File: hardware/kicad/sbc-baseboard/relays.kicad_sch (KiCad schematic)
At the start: 30 parts, among them J11 COM/NO/NC, J12 COM/NO/NC, J18 PSU in (isolated), J19 PSU out (isolated), K801 G6K-2F-Y DC5, K802 G6K-2F-Y DC5, K803 JW1FSN-DC5V, Q801 2N7002, Q802 2N7002, Q803 AO3400A, U801 LTV-817

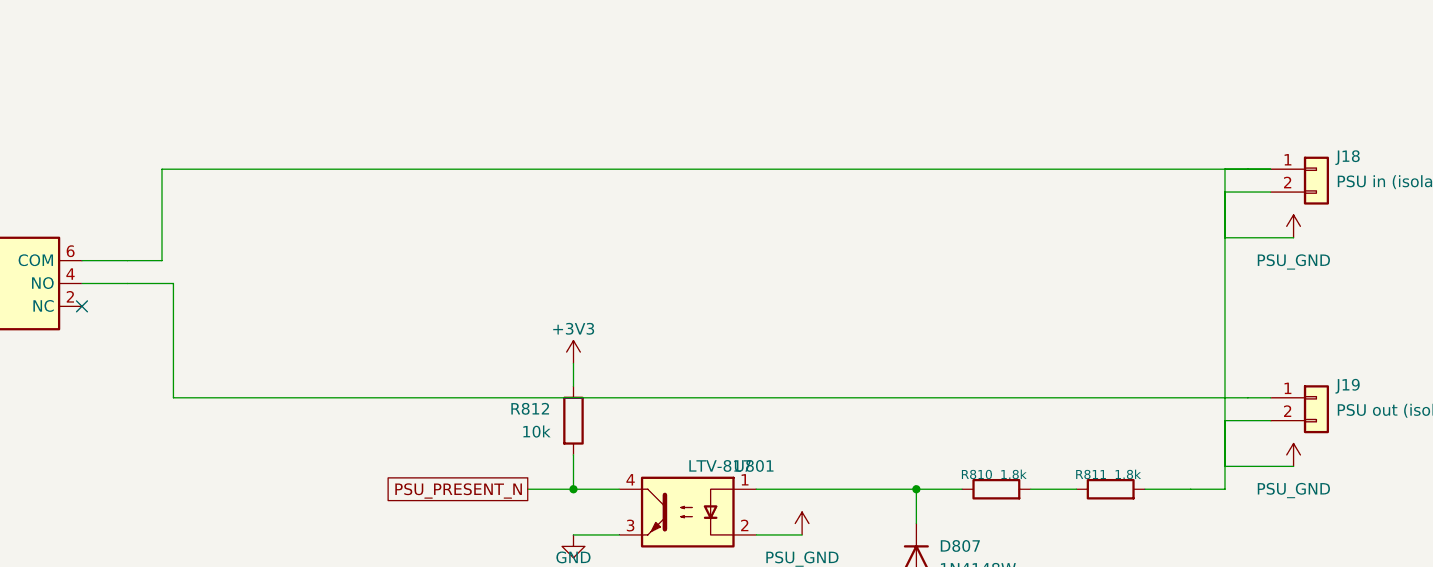
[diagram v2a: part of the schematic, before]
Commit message: USB 2.0 differential pairs named for the router; USB net class; ports aligned
Every USB 2.0 data net is now <base>_P / <base>_N, the suffixes KiCad's PCB
editor pairs up: J1_D, J3_D, PORT1_D..PORT4_D on the receptacle side of each
ESD array; HUB_UP and HUB_DN1..HUB_DN7 at the hub; K64_USB and FTDI_USB at the
chips. All 15 pairs are complete with D+ on _P. The project file gains a USB
net class assigned by pattern (differential geometry to be set from the
stackup). The labels sit at wire ends with their text along the pair's own
wire; routes now run their last leg into a side pin as one wire so a label at
the pin end owns the stretch (Conn join=False keeps a shared stub where two
routes meet at one pin). The USB-A receptacles and their switches move down
1.27 mm so the pairs run straight from the ESD arrays, and the port ESD arrays
move left to make room for the labels. Netlist membership unchanged (356
nets); ERC, geometry, connectivity, layout and reproducibility gates all
clean.

Co-Authored-By: Claude Fable 5.1 <noreply@anthropic.com>
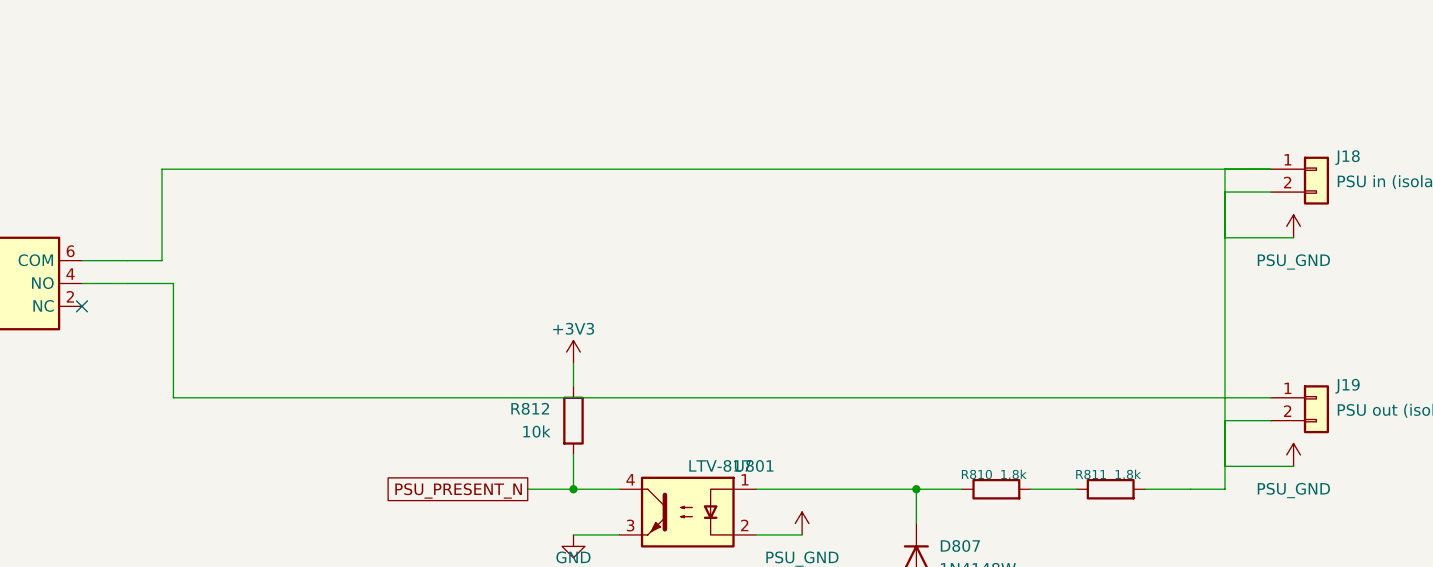
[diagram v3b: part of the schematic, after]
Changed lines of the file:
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@@
 		(pts
 			(xy 171.45 212.09)
-			(xy 292.1 212.09)
-		)
-		(stroke
-			(width 0)
-			(type default)
-		)
-	)
-	(wire
-		(pts
-			(xy 292.1 212.09)
 			(xy 294.64 212.09)
 		)
@@
 		(pts
 			(xy 172.72 237.49)
-			(xy 292.1 237.49)
-		)
-		(stroke
-			(width 0)
-			(type default)
-		)
-	)
-	(wire
-		(pts
-			(xy 292.1 237.49)
 			(xy 294.64 237.49)
 		)
@@
 		(pts
 			(xy 289.56 212.09)
-			(xy 292.1 212.09)
-		)
-		(stroke
-			(width 0)
-			(type default)
-		)
-	)
-	(wire
-		(pts
-			(xy 292.1 212.09)
 			(xy 294.64 212.09)
 		)

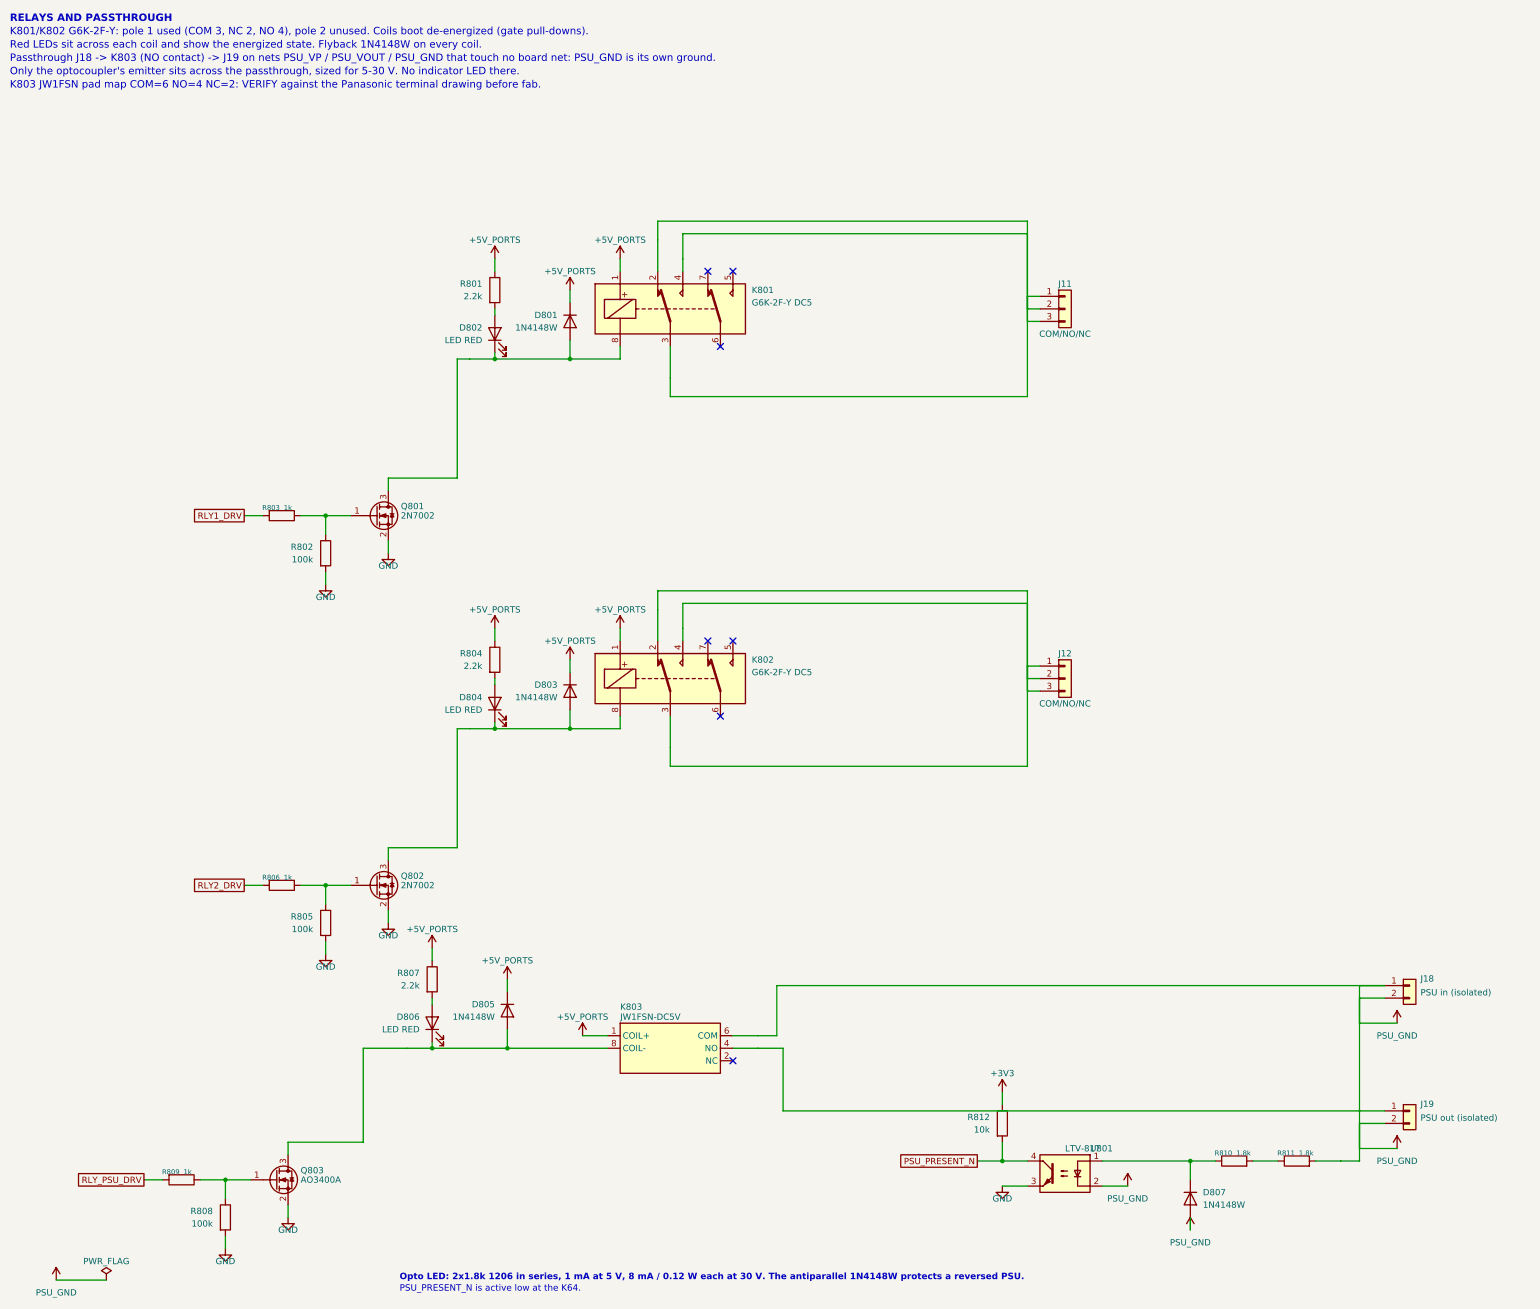
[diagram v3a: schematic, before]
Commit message: Nothing drawn over anything else; FTDI Friend header; DAPLink per FRDM-K64F; 90 ohm USB class
Geometry gate now also reports two wires sharing a stretch, and is at zero on
every sheet. Routes into a stacked connector from one side take staggered
columns and rows; the signal relays are flipped so COM meets the header's
first pin without crossings; the opto-isolator moves above the passthrough
wires and taps the relay's COM lane; a tag before a route ends at the route's
target; routes into joined pins end at the join; the K64's VREGIN diode taps
the VBUS lane beside the ESD's stub; symbol mirrors are applied after
rotation, as KiCad does.

FT231X: the 3V3OUT lane stays on its pin row with its capacitor far out, clear
of the VCC decoupling; J9 mirrors the Adafruit FTDI Friend (VCC 5 V and pin 6
RTS by default on bridged solder jumpers; the first pass had left J9's VCC on
an open jumper only).

DAPLink K20, verified against DAPLink k20dx and the FRDM-K64F OpenSDA circuit:
PTC7 (SWDIO_IN) joins the SWDIO net, 33 R series resistors on the K20's USB
pair (K20_USB_P/N), notes and spec questions 12 and 14 resolved.

USB net class: 0.35 mm / 0.20 mm for 90 ohm on Advanced Circuits' standard
4-layer 62 mil stackup (spec section 8a). ERC 0, geometry 0, merges 0, layout
0, builds reproducible.

Co-Authored-By: Claude Fable 5.1 <noreply@anthropic.com>
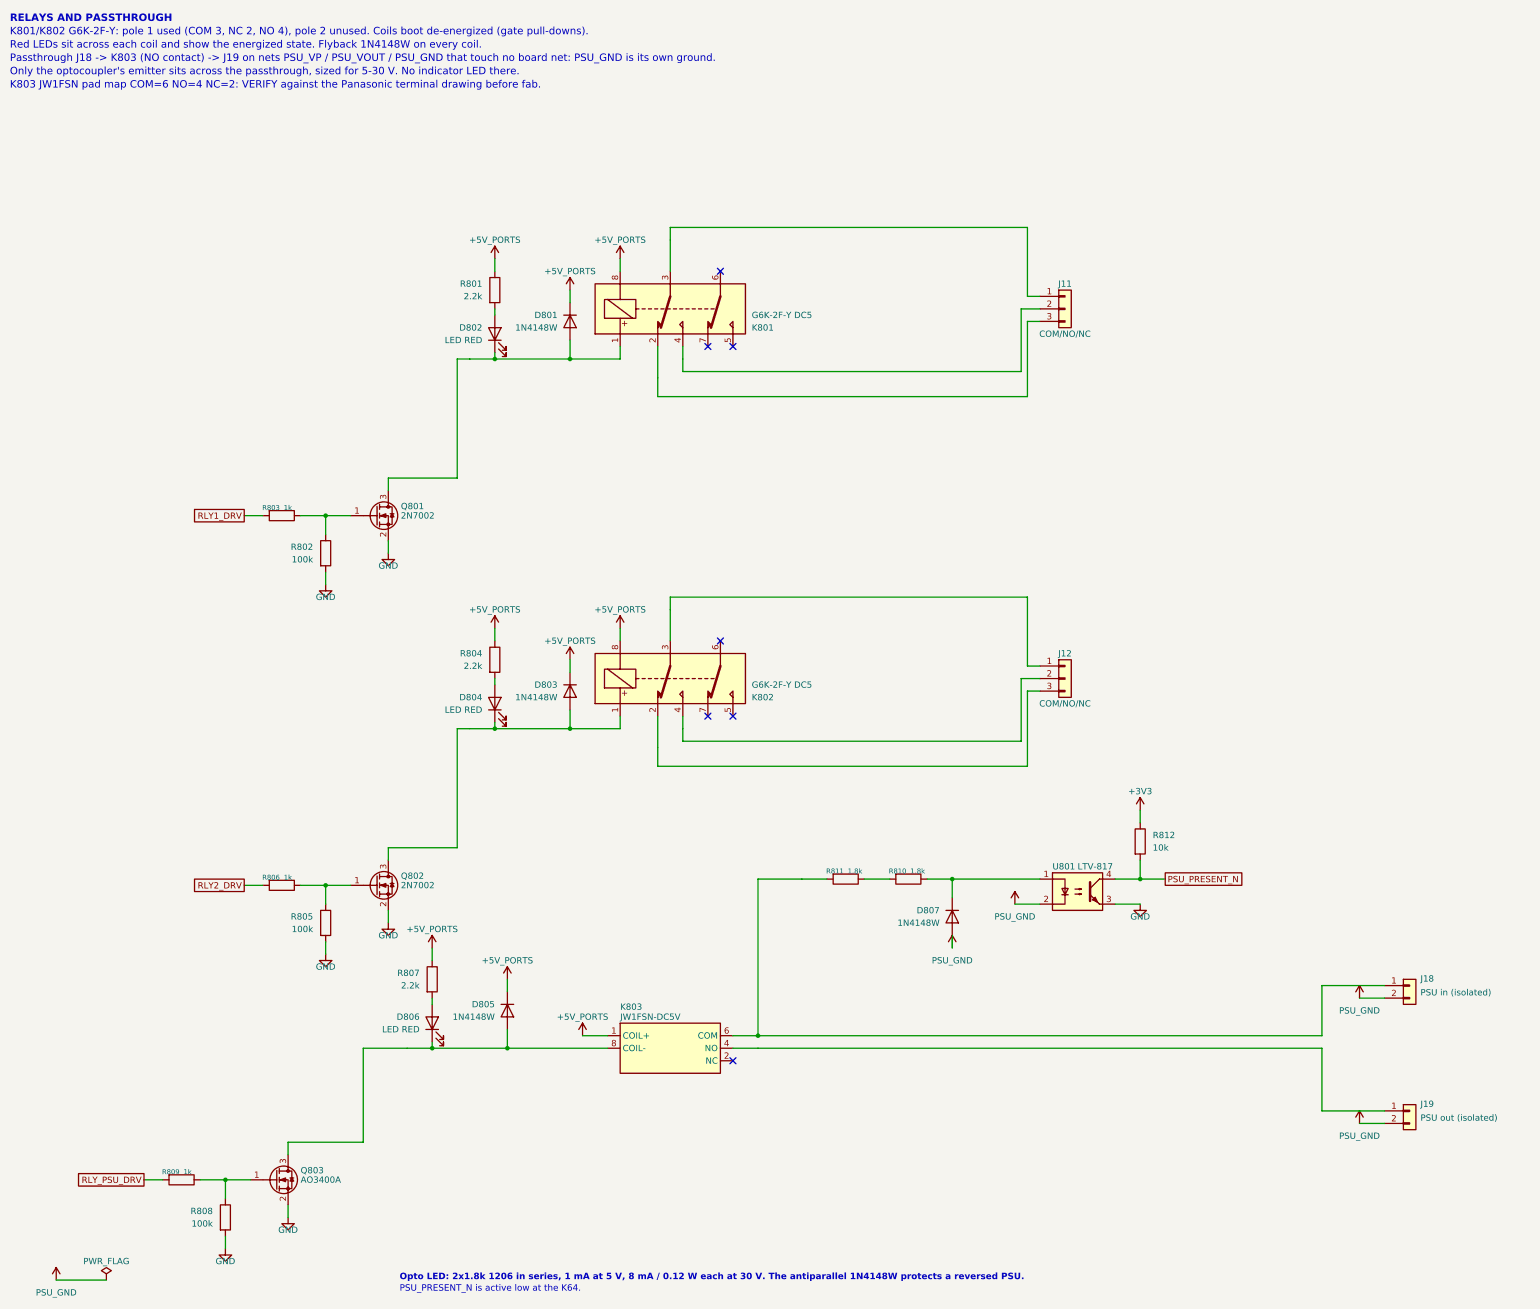
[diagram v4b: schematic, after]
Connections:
- net +5V_PORTS: now also K801.8, K802.8; no longer K801.1, K802.1
- net PSU_GND: no longer J18.1 (Pin_1), K803.6 (COM), R811.2
- net at D803.2 (A), D804.1 (K), Q802.3 (D): now also K802.1; no longer K802.8
- net at D801.2 (A), D802.1 (K), Q801.3 (D): now also K801.1; no longer K801.8
- new net: J11.1 (Pin_1), K801.3
- new net: J11.2 (Pin_2), K801.4
- new net: J11.3 (Pin_3), K801.2
- new net: J12.1 (Pin_1), K802.3
- new net: J12.2 (Pin_2), K802.4
- new net: J12.3 (Pin_3), K802.2
- new net: J18.1 (Pin_1), K803.6 (COM), R811.2
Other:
- moved on the sheet: D807, R810, R811, R812, U801

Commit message: Current pathways annotated on the sheets; net classes PSU_3A, USB_VBUS_3A, PWR_6A; layout directives
Net class directive flags on every high-current net, with the class name
carrying the current: the PSU passthrough (PSU_VP, PSU_VOUT, PSU_GND, now
named), the USB port and FTDI VBUS, VBUS_IN, and the +5V_PORTS / +5V_TGT rails
on the power sheet's flag strip. The project file carries the classes with
their widths and patterns; the XML netlist confirms every net's class. Sheet
notes state the currents and widths. Spec: FTDI header section rewritten for
the Adafruit FTDI Friend defaults (a deliberate exception to the back-feed
rule), current-pathway table in 8a. docs/layout-directives.md written from
the spec for the layout generator.

Co-Authored-By: Claude Fable 5.1 <noreply@anthropic.com>
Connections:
- net PSU_VOUT: now reaches J19.1 (Pin_1), K803.4 (NO)
- net PSU_VP: now reaches J18.1 (Pin_1), K803.6 (COM), R811.2
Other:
- note added: "Current: the passthrough J18 -> K803 -> J19 (PSU_VP, PSU_VOUT, PSU_GND) is laid out for 3 A continuous: class PSU_3A, 2 mm traces or pours, two vias per layer change."
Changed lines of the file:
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@@
 		)
 	)
+	(text "Current: the passthrough J18 -> K803 -> J19 (PSU_VP, PSU_VOUT, PSU_GND) is laid out for 3 A continuous: class PSU_3A, 2 mm traces or pours, two vias per layer change."
+		(exclude_from_sim no)
+		(at 16 33.2 0)
+		(effects
+			(font
+				(size 1.5 1.5)
+			)
+			(justify left bottom)
+		)
+	)
 	(symbol
 		(lib_id "Relay:G6K-2")
@@
 		(pts
 			(xy 289.56 212.09)
-			(xy 281.94 212.09)
+			(xy 278.13 212.09)
 		)
 		(stroke
@@
 	(wire
 		(pts
-			(xy 281.94 212.09)
-			(xy 281.94 222.25)
+			(xy 278.13 212.09)
+			(xy 278.13 222.25)
 		)
 		(stroke
@@
 	(wire
 		(pts
-			(xy 281.94 222.25)
+			(xy 278.13 222.25)
 			(xy 167.64 222.25)
 		)
@@
 		(pts
 			(xy 289.56 237.49)
-			(xy 281.94 237.49)
+			(xy 278.13 237.49)
 		)
 		(stroke
@@
 	(wire
 		(pts
-			(xy 281.94 237.49)
-			(xy 281.94 224.79)
+			(xy 278.13 237.49)
+			(xy 278.13 224.79)
 		)
 		(stroke
@@
 	(wire
 		(pts
-			(xy 281.94 224.79)
+			(xy 278.13 224.79)
 			(xy 167.64 224.79)
 		)
@@
 		)
 	)
+	(label "PSU_VP"
+		(at 289.56 212.09 180)
+		(fields_autoplaced yes)
+		(effects
+			(font
+				(size 1.27 1.27)
+			)
+			(justify right bottom)
+		)
+	)
+	(netclass_flag ""
+		(length 2.54)
+		(shape round)
+		(at 289.56 212.09 90)
+		(fields_autoplaced no)
+		(effects
+			(font
+				(size 1.27 1.27)
+			)
+			(justify left bottom)
+		)
+		(property "Netclass" "PSU_3A"
+			(at 290.56 209.25 0)
+			(effects
+				(font
+					(size 1.27 1.27)
+					(italic yes)
+				)
+				(justify left)
+			)
+		)
+	)
+	(label "PSU_VOUT"
+		(at 289.56 237.49 180)
+		(fields_autoplaced yes)
+		(effects
+			(font
+				(size 1.27 1.27)
+			)
+			(justify right bottom)
+		)
+	)
+	(netclass_flag ""
+		(length 2.54)
+		(shape round)
+		(at 289.56 237.49 90)
+		(fields_autoplaced no)
+		(effects
+			(font
+				(size 1.27 1.27)
+			)
+			(justify left bottom)
+		)
+		(property "Netclass" "PSU_3A"
+			(at 290.56 234.65 0)
+			(effects
+				(font
+					(size 1.27 1.27)
+					(italic yes)
+				)
+				(justify left)
+			)
+		)
+	)
 	(wire
 		(pts
@@
 		(pts
 			(xy 25.4 271.78)
+			(xy 30.48 271.78)
+		)
+		(stroke
+			(width 0)
+			(type default)
+		)
+	)
+	(wire
+		(pts
+			(xy 30.48 271.78)
 			(xy 35.56 271.78)
 		)
@@
 		)
 	)
+	(netclass_flag ""
+		(length 2.54)
+		(shape round)
+		(at 30.48 271.78 270)
+		(fields_autoplaced no)
+		(effects
+			(font
+				(size 1.27 1.27)
+			)
+			(justify left bottom)
+		)
+		(property "Netclass" "PSU_3A"
+			(at 31.48 275.52 0)
+			(effects
+				(font
+					(size 1.27 1.27)
+					(italic yes)
+				)
+				(justify left)
+			)
+		)
+	)
